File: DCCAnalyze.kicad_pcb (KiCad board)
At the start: 2 copper layers, 117 x 62 mm, 31 parts, among them J1 RJ12, SW1 PWR_SEL, SW2 LEFT, SW3 UP, SW4 RIGHT, U1 6N137, U2 6N137

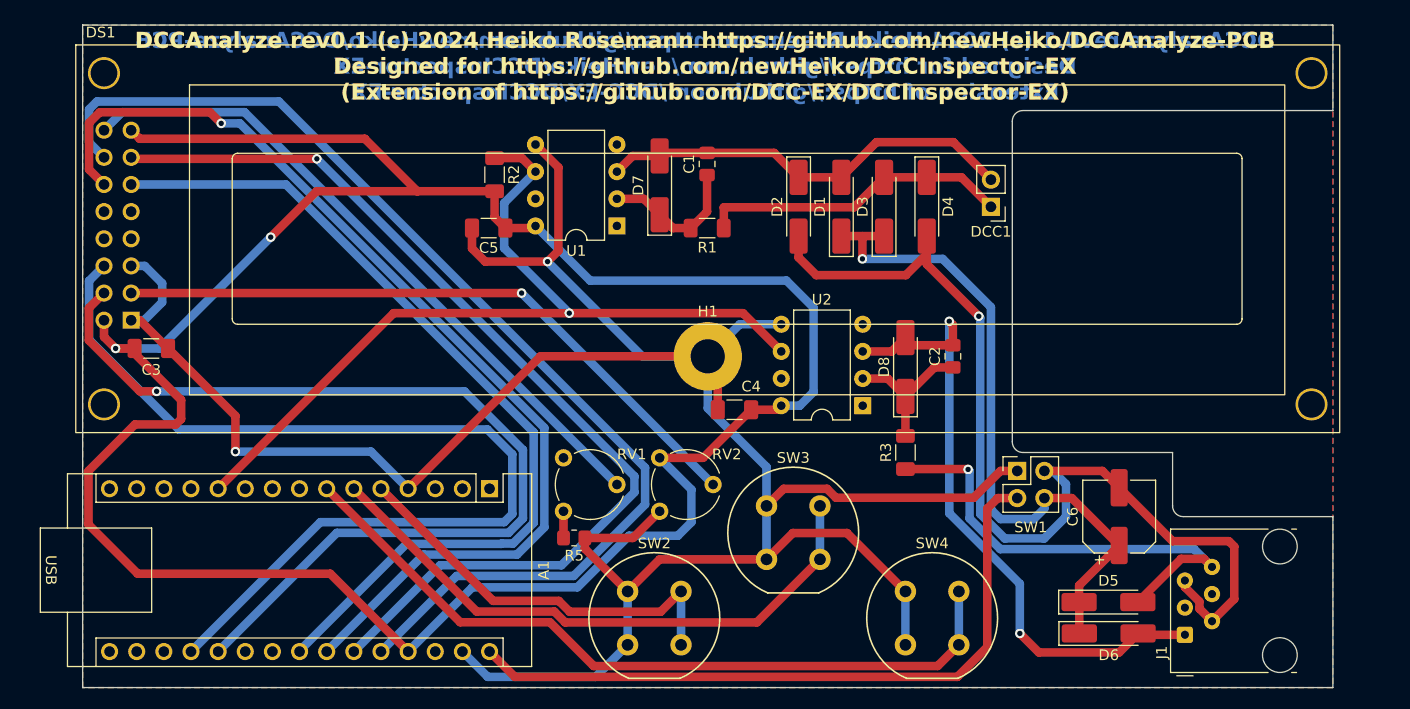
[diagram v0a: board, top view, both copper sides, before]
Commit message: Move RJ12 connector inwards to match housing.
...for rev0.2
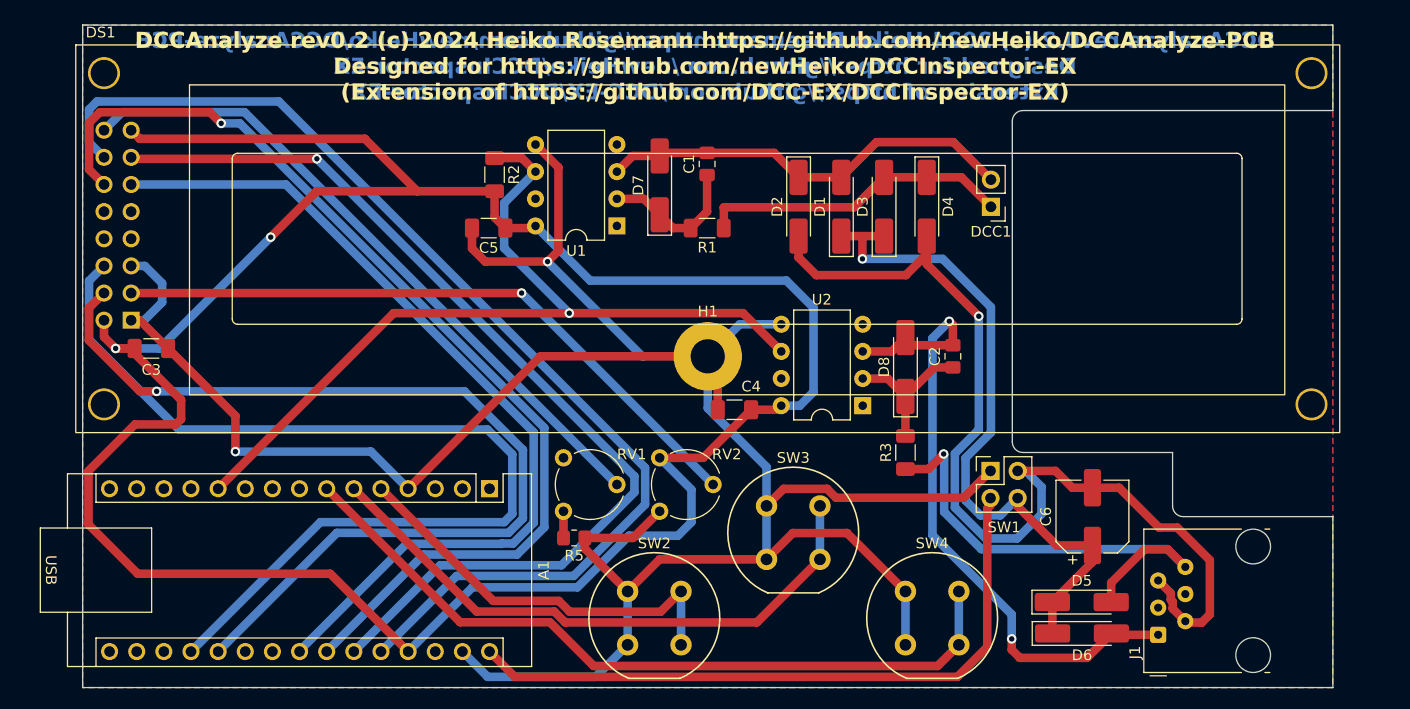
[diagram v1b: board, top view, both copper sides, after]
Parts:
- moved C6 2.50 mm to (194.5, 96.0)
- moved D5 2.50 mm to (193.5, 104.0)
- moved D6 2.50 mm to (193.5, 106.9)
- moved J1 2.50 mm to (200.7, 107.1)
- moved SW1 2.50 mm to (185.0, 91.7)
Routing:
- net GND: track 248.8 -> 246.3 mm
- net Net-(A1-VIN): track 64.9 -> 62.8 mm
- net GND1: track 94.1 -> 95.2 mm
- net Net-(D5-A): track 44.0 -> 45.0 mm
- net Net-(D6-A): track 60.6 -> 61.1 mm
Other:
- board text added: "DCCAnalyze rev0.2 (c) 2024 Heiko Rosemann https://github.com/newHeiko/DCCAnalyze-PCB Designed for https://github.com/newHeiko/DCCInspector-EX (Extension of https://github.com/DCC-EX/DCCInspector-EX)"
- board text removed: "DCCAnalyze rev0.1 (c) 2024 Heiko Rosemann https://github.com/newHeiko/DCCAnalyze-PCB Designed for https://github.com/newHeiko/DCCInspector-EX (Extension of https://github.com/DCC-EX/DCCInspector-EX)"

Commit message: Correct LCD value
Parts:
- DS1: value WC1602A -> LCD242
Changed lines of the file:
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@@
 			)
 		)
-		(property "Value" "WC1602A"
+		(property "Value" "LCD242"
 			(at -1.35 11.54 0)
 			(layer "F.Fab")
@@
 			)
 		)
-		(property "Description" "LCD 16x2 Alphanumeric , 8 bit parallel bus, 5V VDD"
+		(property "Description" "LCD 24x2 Alphanumeric , 8 bit parallel bus, 5V VDD"
 			(at 2.96 -23.12 0)
 			(unlocked yes)
@@
 			)
 		)
+		(property ki_fp_filters "*WC*1602A*")
+		(sheetname "Root")
+		(sheetfile "DCCAnalyze.kicad_sch")
 		(attr through_hole)
 		(fp_line
@@
 			)
 		)
+		(property ki_fp_filters "Arduino*Nano*")
+		(sheetname "Root")
+		(sheetfile "DCCAnalyze.kicad_sch")
 		(attr through_hole)
 		(fp_line
